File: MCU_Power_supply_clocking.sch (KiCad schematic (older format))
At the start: 60 parts, among them U6 STM32H743ZIT6, Y2 NX5032GA-8MHz, Y3 NX3215SA-32.768K-STD-MUA-14

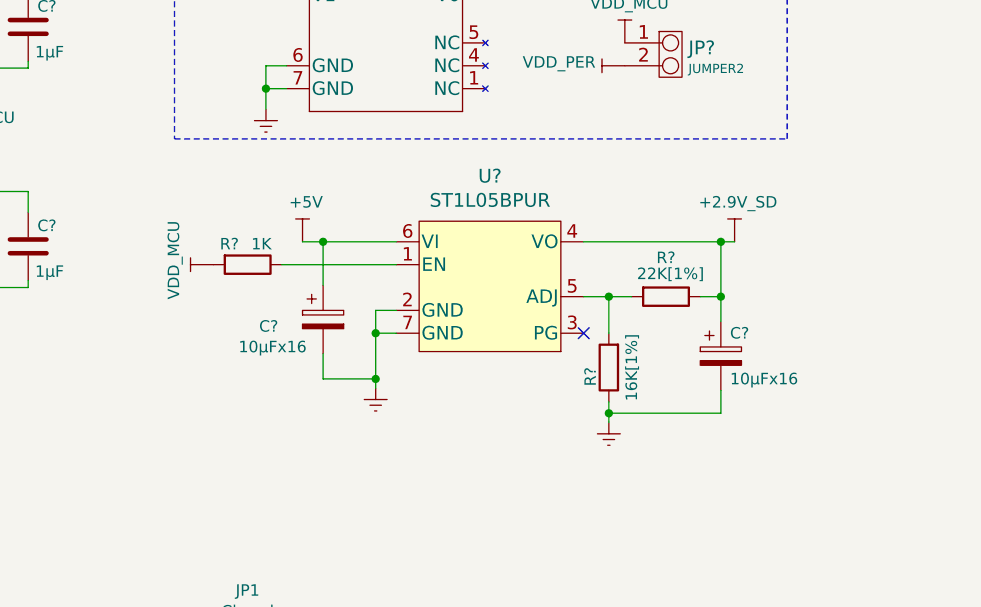
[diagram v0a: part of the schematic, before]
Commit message: Added SD_Card Tranceiver TXS0206-29. Deleted2.9V LDO
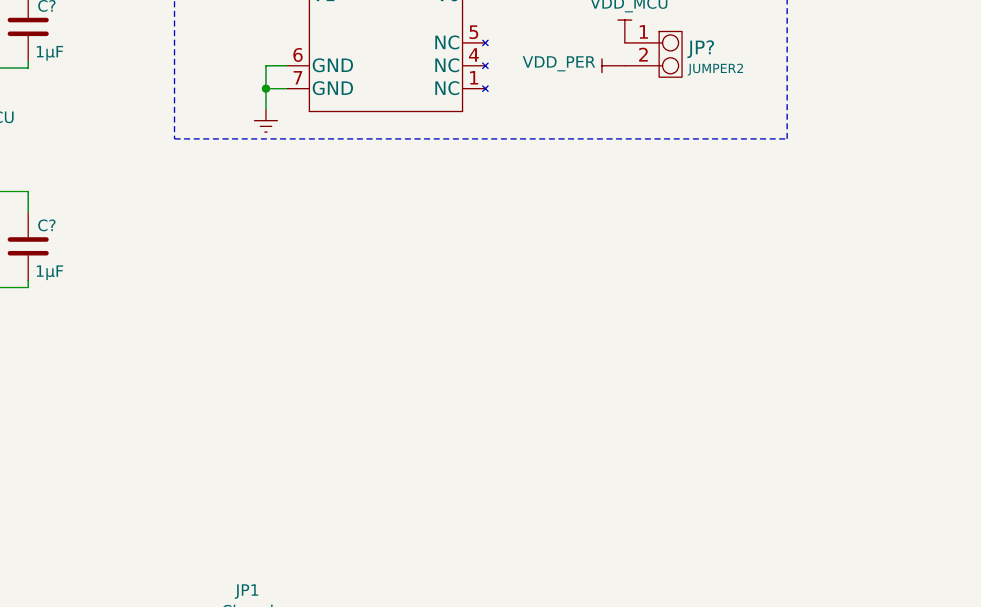
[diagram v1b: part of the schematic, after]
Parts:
- removed C? (x2): 10µFx16, symbol Device:CP
- removed R?: 1K, Resistor_SMD:R_0805_2012Metric_Pad1.20x1.40mm_HandSolder, symbol Device:R
- removed R?: 22K[1%], Resistor_SMD:R_0805_2012Metric_Pad1.20x1.40mm_HandSolder, symbol Device:R
- removed R?: 16K[1%], Resistor_SMD:R_0805_2012Metric_Pad1.20x1.40mm_HandSolder, symbol Device:R
- removed U?: ST1L05BPUR, SVIELCOM:ST1L05BPUR, symbol SVIELCOM_Library:ST1L05BPUR
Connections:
- no-connect marks 1 -> 0
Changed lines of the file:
@@
 $EndComp
-$Comp
-L SVIELCOM_Library:ST1L05BPUR U?
-U 1 1 6096844B
-P 8540 2460
-F 0 "U?" H 9150 2847 60  0000 C CNN
-F 1 "ST1L05BPUR" H 9150 2741 60  0000 C CNN
-F 2 "SVIELCOM:ST1L05BPUR" H 9110 2010 60  0001 C CNN
-F 3 "https://my.st.com/resource/en/datasheet/st1l05.pdf" H 9150 2741 60  0001 C CNN
-	1    8540 2460
-	1    0    0    -1
-$EndComp
-NoConn ~ 9560 2760
 $Comp
 L SVIELCOM_Library:+5V #PWR?
@@
 Backup LDO
 $Comp
-L power:GNDREF #PWR?
-U 1 1 60B41EE3
-P 8650 3000
-AR Path="/60B41EE3" Ref="#PWR?"  Part="1"
-AR Path="/60A03F8A/60B41EE3" Ref="#PWR?"  Part="1"
-F 0 "#PWR?" H 8650 2750 50  0001 C CNN
-F 1 "GNDREF" V 8655 2872 50  0001 R CNN
-F 2 "" H 8650 3000 50  0001 C CNN
-F 3 "" H 8650 3000 50  0001 C CNN
-	1    8650 3000
-	1    0    0    -1
-$EndComp
-Wire Wire Line
-	8650 3000 8650 2960
-Wire Wire Line
-	8650 2660 8740 2660
-Wire Wire Line
-	8740 2760 8650 2760
-Connection ~ 8650 2760
-Wire Wire Line
-	8650 2760 8650 2660
-$Comp
-L SVIELCOM_Library:+5V #PWR?
-U 1 1 60B6234A
-P 8330 2360
-F 0 "#PWR?" H 8330 2210 50  0001 C CNN
-F 1 "+5V" H 8345 2533 50  0000 C CNN
-F 2 "" H 8330 2360 50  0001 C CNN
-F 3 "" H 8330 2360 50  0001 C CNN
-	1    8330 2360
-	1    0    0    -1
-$EndComp
-$Comp
-L Device:R R?
-U 1 1 60B72F6C
-P 8090 2460
-AR Path="/60B72F6C" Ref="R?"  Part="1"
-AR Path="/60A03F8A/60B72F6C" Ref="R?"  Part="1"
-F 0 "R?" V 8000 2380 50  0000 C CNN
-F 1 "1K" V 8000 2520 50  0000 C CNN
-F 2 "Resistor_SMD:R_0805_2012Metric_Pad1.20x1.40mm_HandSolder" V 8020 2460 50  0001 C CNN
-F 3 "~" H 8090 2460 50  0001 C CNN
-	1    8090 2460
-	0    1    1    0
-$EndComp
-$Comp
-L Device:CP C?
-U 1 1 60B74100
-P 8420 2700
-AR Path="/60B74100" Ref="C?"  Part="1"
-AR Path="/60A03F8A/60B74100" Ref="C?"  Part="1"
-F 0 "C?" H 8140 2670 50  0000 L CNN
-F 1 "10µFx16" H 8050 2580 50  0000 L CNN
-F 2 "" H 8458 2550 50  0001 C CNN
-F 3 "" H 8420 2700 50  0001 C CNN
-F 4 "593D106X9016A2TE3" H 8420 2700 50  0001 C CNN "Type"
-	1    8420 2700
-	1    0    0    -1
-$EndComp
-$Comp
-L SVIELCOM_Library:VDD_MCU #PWR?
-U 1 1 60BA614F
-P 7940 2460
-AR Path="/60BA614F" Ref="#PWR?"  Part="1"
-AR Path="/60A03F8A/60BA614F" Ref="#PWR?"  Part="1"
-F 0 "#PWR?" H 7940 2310 50  0001 C CNN
-F 1 "VDD_MCU" H 7960 2633 50  0000 C CNN
-F 2 "" H 7940 2460 50  0001 C CNN
-F 3 "" H 7940 2460 50  0001 C CNN
-	1    7940 2460
-	0    -1   -1   0
-$EndComp
-Wire Wire Line
-	8240 2460 8740 2460
-$Comp
-L Device:R R?
-U 1 1 60BBA878
-P 9920 2600
-AR Path="/60BBA878" Ref="R?"  Part="1"
-AR Path="/60A03F8A/60BBA878" Ref="R?"  Part="1"
-F 0 "R?" V 9750 2600 50  0000 C CNN
-F 1 "22K[1%]" V 9820 2620 50  0000 C CNN
-F 2 "Resistor_SMD:R_0805_2012Metric_Pad1.20x1.40mm_HandSolder" V 9850 2600 50  0001 C CNN
-F 3 "~" H 9920 2600 50  0001 C CNN
-	1    9920 2600
-	0    1    1    0
-$EndComp
-$Comp
-L Device:R R?
-U 1 1 60BBB173
-P 9670 2910
-AR Path="/60BBB173" Ref="R?"  Part="1"
-AR Path="/60A03F8A/60BBB173" Ref="R?"  Part="1"
-F 0 "R?" V 9750 2950 50  0000 C CNN
-F 1 "16K[1%]" V 9570 2910 50  0000 C CNN
-F 2 "Resistor_SMD:R_0805_2012Metric_Pad1.20x1.40mm_HandSolder" V 9600 2910 50  0001 C CNN
-F 3 "~" H 9670 2910 50  0001 C CNN
-	1    9670 2910
-	-1   0    0    1
-$EndComp
-Wire Wire Line
-	9560 2600 9670 2600
-Wire Wire Line
-	9670 2760 9670 2600
-Connection ~ 9670 2600
-Wire Wire Line
-	9670 2600 9770 2600
-$Comp
-L power:GNDREF #PWR?
-U 1 1 60BED935
-P 9670 3150
-AR Path="/60BED935" Ref="#PWR?"  Part="1"
-AR Path="/60A03F8A/60BED935" Ref="#PWR?"  Part="1"
-F 0 "#PWR?" H 9670 2900 50  0001 C CNN
-F 1 "GNDREF" V 9675 3022 50  0001 R CNN
-F 2 "" H 9670 3150 50  0001 C CNN
-F 3 "" H 9670 3150 50  0001 C CNN
-	1    9670 3150
-	1    0    0    -1
-$EndComp
-Wire Wire Line
-	9670 3150 9670 3110
-Wire Wire Line
-	9560 2360 10160 2360
-Wire Wire Line
-	10160 2360 10160 2600
-Wire Wire Line
-	10160 2600 10070 2600
-$Comp
-L Device:CP C?
-U 1 1 60C10398
-P 10160 2860
-AR Path="/60C10398" Ref="C?"  Part="1"
-AR Path="/60A03F8A/60C10398" Ref="C?"  Part="1"
-F 0 "C?" H 10200 2960 50  0000 L CNN
-F 1 "10µFx16" H 10200 2760 50  0000 L CNN
-F 2 "" H 10198 2710 50  0001 C CNN
-F 3 "" H 10160 2860 50  0001 C CNN
-F 4 "593D106X9016A2TE3" H 10160 2860 50  0001 C CNN "Type"
-	1    10160 2860
-	1    0    0    -1
-$EndComp
-Wire Wire Line
-	10160 2710 10160 2600
-Connection ~ 10160 2600
-Wire Wire Line
-	9670 3110 10160 3110
-Wire Wire Line
-	10160 3110 10160 3010
-Connection ~ 9670 3110
-Wire Wire Line
-	9670 3110 9670 3060
-$Comp
-L SVIELCOM_Library:+2.9V_SD #PWR?
-U 1 1 60C4B601
-P 10220 2360
-F 0 "#PWR?" H 10220 2210 50  0001 C CNN
-F 1 "+2.9V_SD" H 10235 2533 50  0000 C CNN
-F 2 "" H 10220 2360 50  0001 C CNN
-F 3 "" H 10220 2360 50  0001 C CNN
-	1    10220 2360
-	1    0    0    -1
-$EndComp
-Wire Wire Line
-	10160 2360 10220 2360
-Connection ~ 10160 2360
-Wire Wire Line
-	8330 2360 8420 2360
-Wire Wire Line
-	8420 2550 8420 2360
-Connection ~ 8420 2360
-Wire Wire Line
-	8420 2360 8740 2360
-Wire Wire Line
-	8420 2960 8650 2960
-Connection ~ 8650 2960
-Wire Wire Line
-	8650 2960 8650 2760
-Wire Wire Line
-	8420 2850 8420 2960
-$Comp
 L freetronics_schematic:JUMPER2 JP?

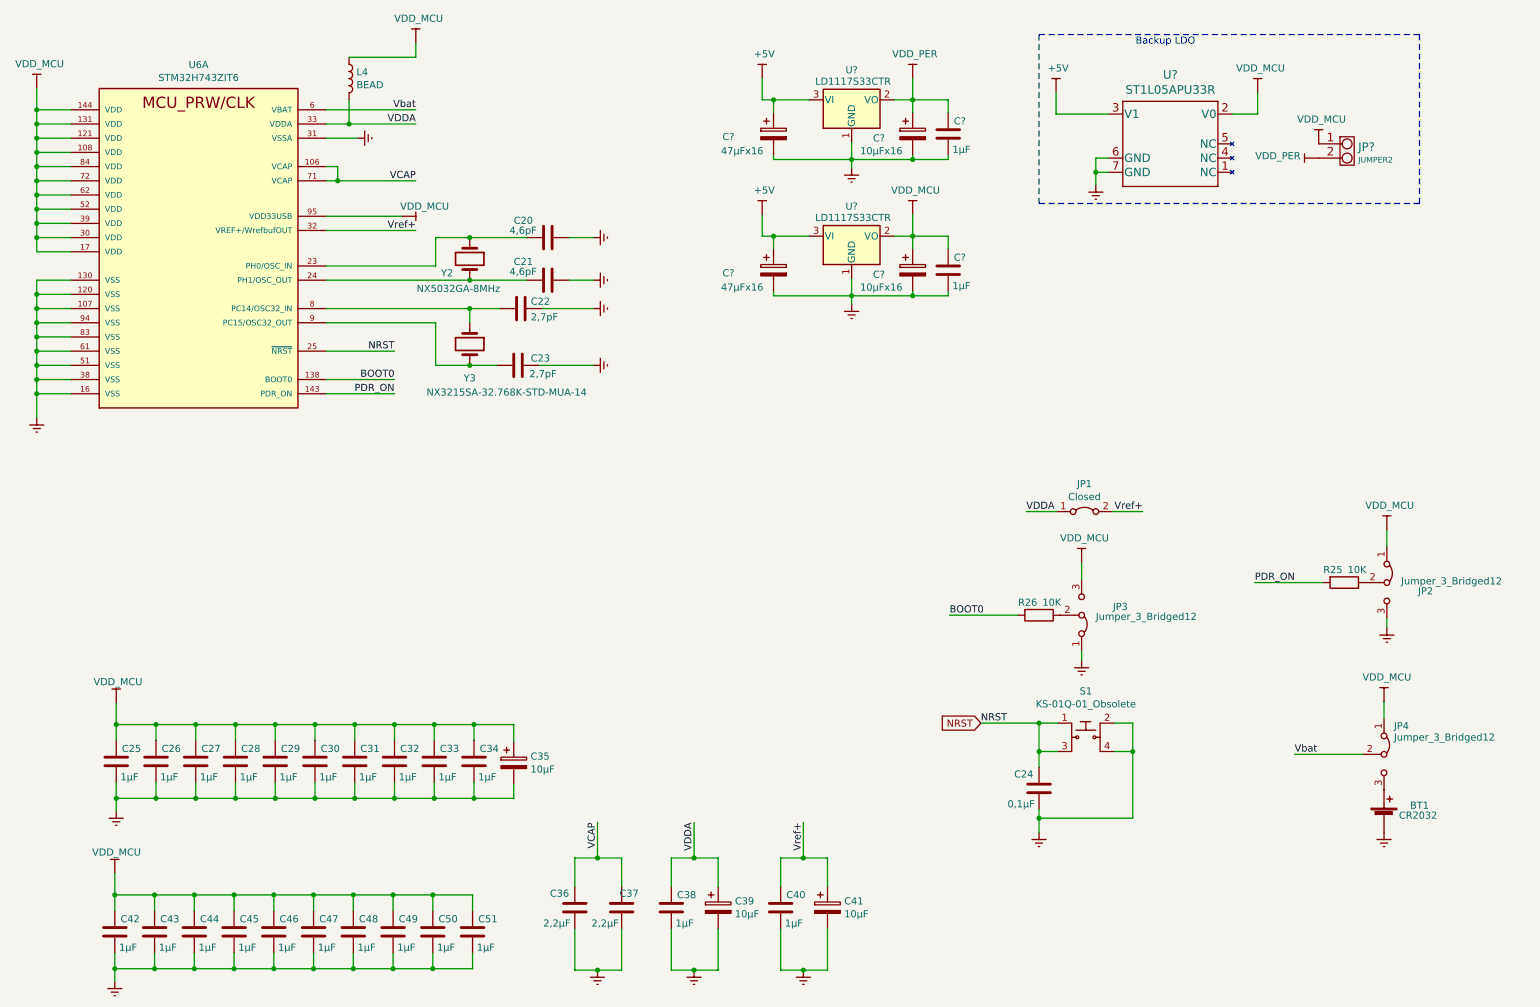
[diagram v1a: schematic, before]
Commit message: Restore 2.9V LDO
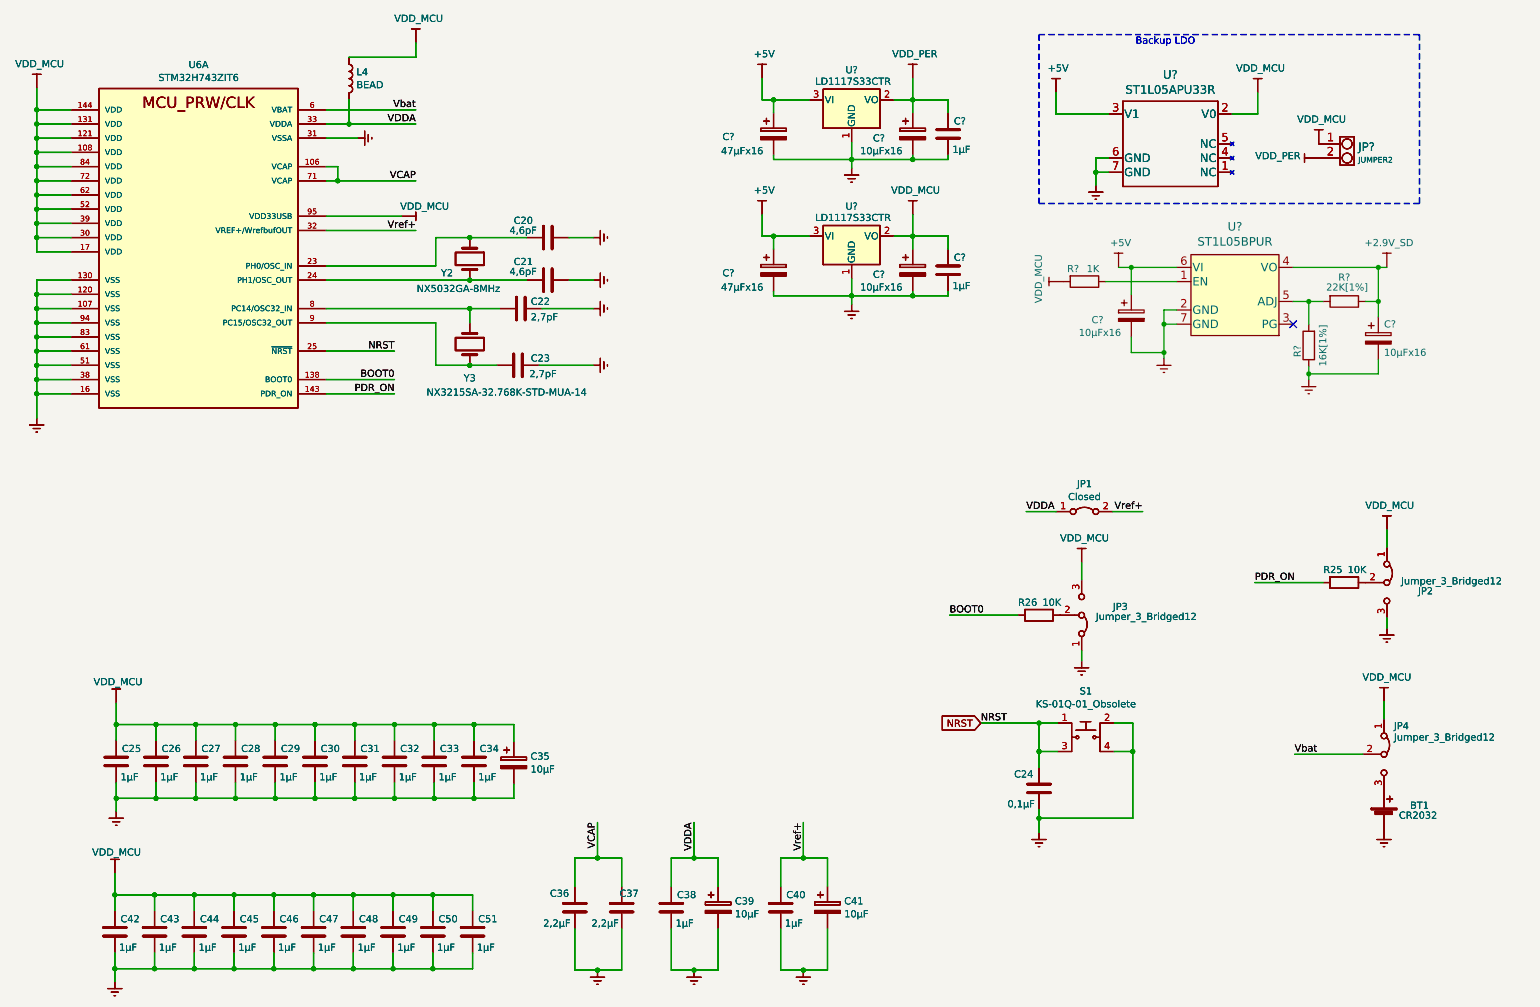
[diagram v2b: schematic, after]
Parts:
- added BT1: CR2032, symbol Device:Battery_Cell
- added C20, C21: 4,6pF, Capacitor_SMD:C_0603_1608Metric_Pad1.08x0.95mm_HandSolder, symbol Device:C
- added C22, C23: 2,7pF, Capacitor_SMD:C_0603_1608Metric_Pad1.08x0.95mm_HandSolder, symbol Device:C
- added C24: 0,1µF, Capacitor_SMD:C_0805_2012Metric_Pad1.18x1.45mm_HandSolder, symbol Device:C
- added C25, C26, C27, C28, C29, C30, C31, C32, C33, C34, C38, C40, C42, C43, C44, C45, C46, C47, C48, C49, C50, C51, C? (x2): 1µF, Capacitor_SMD:C_0603_1608Metric_Pad1.08x0.95mm_HandSolder, symbol Device:C
- added C35, C39, C41: 10µF, Capacitor_Tantalum_SMD:CP_EIA-3216-10_Kemet-I, symbol Device:CP
- added C36, C37: 2,2µF, Capacitor_SMD:C_0805_2012Metric_Pad1.18x1.45mm_HandSolder, symbol Device:C
- added C? (x2): 47µFx16, Capacitor_Tantalum_SMD:CP_EIA-7343-31_Kemet-D_Pad2.25x2.55mm_HandSolder, symbol Device:CP
- added C? (x4): 10µFx16, symbol Device:CP
- added JP1: Closed, symbol Jumper:Jumper_2_Bridged
- added JP2, JP3, JP4: Jumper_3_Bridged12, symbol Jumper:Jumper_3_Bridged12
- added JP?: JUMPER2, symbol freetronics_schematic:JUMPER2
- added L4: BEAD, symbol Device:L
- added R25, R26: 10K, Resistor_SMD:R_0805_2012Metric_Pad1.20x1.40mm_HandSolder, symbol Device:R
- added R?: 1K, Resistor_SMD:R_0805_2012Metric_Pad1.20x1.40mm_HandSolder, symbol Device:R
- added R?: 22K[1%], Resistor_SMD:R_0805_2012Metric_Pad1.20x1.40mm_HandSolder, symbol Device:R
- added R?: 16K[1%], Resistor_SMD:R_0805_2012Metric_Pad1.20x1.40mm_HandSolder, symbol Device:R
- added S1: KS-01Q-01_Obsolete, digikey-footprints:PushButton_Round_D12mm_THT_KS-01Q-01, symbol dk_Pushbutton-Switches:KS-01Q-01_Obsolete
- added U6: STM32H743ZIT6, QFP50P2200X2200X160-144N, symbol SVIELCOM_Library:STM32H743ZIT6
- added U?: ST1L05BPUR, SVIELCOM:ST1L05BPUR, symbol SVIELCOM_Library:ST1L05BPUR
- added U? (x2): LD1117S33CTR, Package_TO_SOT_SMD:SOT-223-3_TabPin2, symbol Regulator_Linear:LD1117S33TR_SOT223
- added U?: ST1L05APU33R, DFN_5APU33R_STM, symbol SVIELCOM_Library:ST1L05APU33R
- added Y2: NX5032GA-8MHz, Crystal:Crystal_SMD_5032-2Pin_5.0x3.2mm_HandSoldering, symbol Device:Crystal
- added Y3: NX3215SA-32.768K-STD-MUA-14, Crystal:Crystal_SMD_MicroCrystal_CC7V-T1A-2Pin_3.2x1.5mm_HandSoldering, symbol Device:Crystal
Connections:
- net +5V: now also C?.1, C?.1, C?.1, U?.3 (V1), U?.3 (VI), U?.3 (VI), U?.6 (VI)
- net BOOT0: now also R26.2, U6.138 (BOOT0)
- net GNDREF: now also BT1.2 (-), C20.1, C21.1, C22.1, C23.1, C24.1, C25.2, C26.2, C27.2, C28.2, C29.2, C30.2, C31.2, C32.2, C33.2, C34.2, C35.2, C36.1, C37.1, C38.2, C39.2, C40.2, C41.2, C42.2, C43.2, C44.2, C45.2, C46.2, C47.2, C48.2, C49.2, C50.2, C51.2, C?.2, C?.2, C?.2, C?.2, C?.2, C?.2, C?.2, C?.2, JP2.3 (B), JP3.1 (A), R?.1, S1.2, S1.4, U6.107 (VSS), U6.120 (VSS), U6.130 (VSS), U6.16 (VSS), U6.31 (VSSA), U6.38 (VSS), U6.51 (VSS), U6.61 (VSS), U6.83 (VSS), U6.94 (VSS), U?.1 (GND), U?.1 (GND), U?.2 (GND), U?.6 (GND), U?.7 (GND), U?.7 (GND)
- net NRST: now also C24.2, S1.1, S1.3, U6.25 (~NRST)
- net PDR_ON: now also R25.2, U6.143 (PDR_ON)
- net VCAP: now also C36.2, C37.2, U6.106 (VCAP), U6.71 (VCAP)
- net VDDA: now also C38.1, C39.1, JP1.1 (A), L4.2, U6.33 (VDDA)
- net VDD_MCU: now also C25.1, C26.1, C27.1, C28.1, C29.1, C30.1, C31.1, C32.1, C33.1, C34.1, C35.1, C42.1, C43.1, C44.1, C45.1, C46.1, C47.1, C48.1, C49.1, C50.1, C51.1, C?.1, C?.1, JP2.1 (A), JP3.3 (B), JP4.1 (A), JP?.1, L4.1, R?.2, U6.108 (VDD), U6.121 (VDD), U6.131 (VDD), U6.144 (VDD), U6.17 (VDD), U6.30 (VDD), U6.39 (VDD), U6.52 (VDD), U6.62 (VDD), U6.72 (VDD), U6.84 (VDD), U6.95 (VDD33USB), U?.2 (V0), U?.2 (VO)
- net VDD_PER: now also C?.1, C?.1, JP?.2, U?.2 (VO)
- net Vbat: now also JP4.2 (C), U6.6 (VBAT)
- net Vref+: now also C40.1, C41.1, JP1.2 (B), U6.32 (VREF+/WrefbufOUT)
- net at C22.2, U6.8 (PC14/OSC32_IN), Y3.1: now also C22.2, U6.8 (PC14/OSC32_IN), Y3.1
- net at C23.2, U6.9 (PC15/OSC32_OUT), Y3.2: now also C23.2, U6.9 (PC15/OSC32_OUT), Y3.2
- net at C20.2, U6.23 (PH0/OSC_IN), Y2.1: now also C20.2, U6.23 (PH0/OSC_IN), Y2.1
- net at C21.2, U6.24 (PH1/OSC_OUT), Y2.2: now also C21.2, U6.24 (PH1/OSC_OUT), Y2.2
- net at JP3.2 (C), R26.1: now also JP3.2 (C), R26.1
- net at BT1.1 (+), JP4.3 (B): now also BT1.1 (+), JP4.3 (B)
- net at U?.1 (NC): now also U?.1 (NC)
- net at U?.4 (NC): now also U?.4 (NC)
- net at U?.5 (NC): now also U?.5 (NC)
- net at JP2.2 (C), R25.1: now also JP2.2 (C), R25.1
- new net: R?.1, U?.1 (EN)
- new net: R?.2, R?.2, U?.5 (ADJ)
- new net +2,9V: C?.1, R?.1, U?.4 (VO)
- no-connect marks 0 -> 1
